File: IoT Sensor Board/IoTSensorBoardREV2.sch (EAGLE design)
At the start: 29 parts, among them Q1 BCW32SMD, Q2 BCW32SMD, U2 3.3V

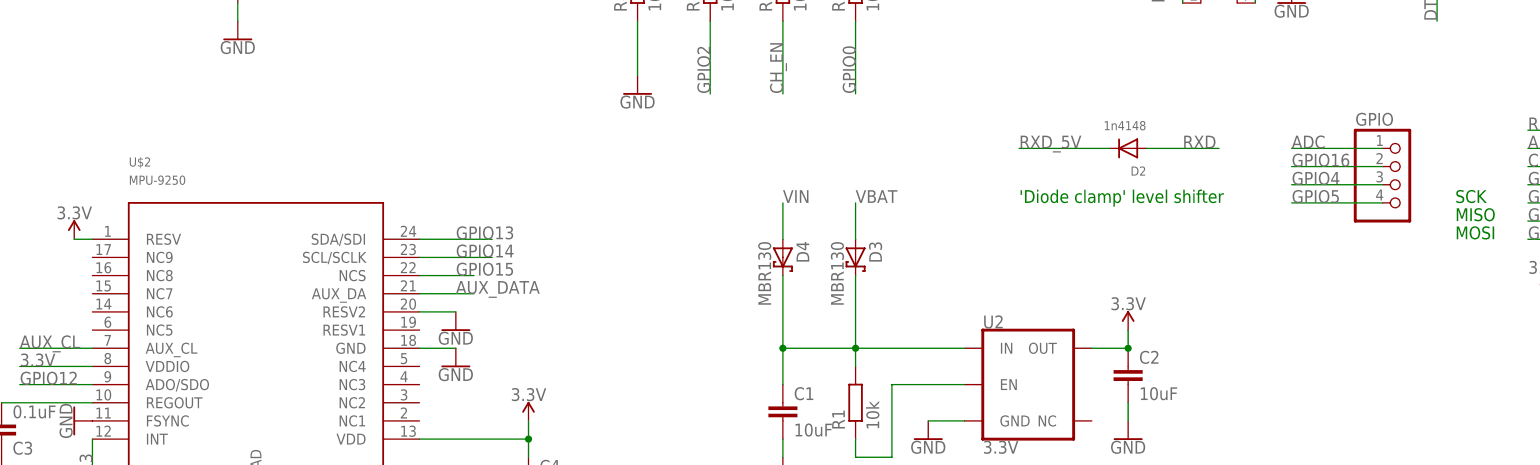
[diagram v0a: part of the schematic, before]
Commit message: Updated REV2
Silkscreen improved
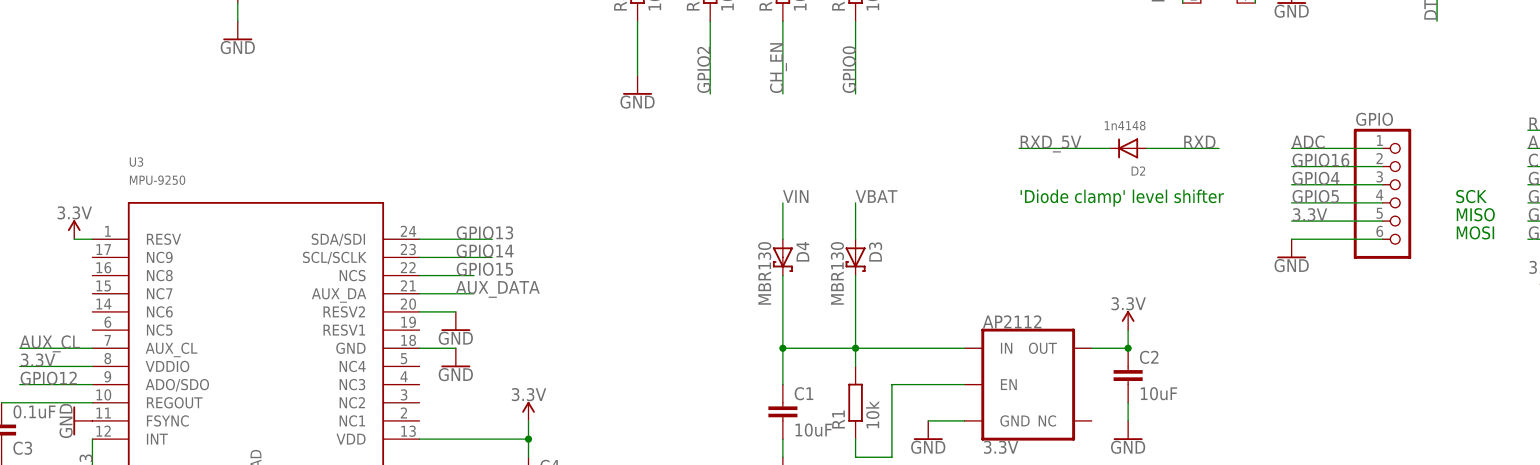
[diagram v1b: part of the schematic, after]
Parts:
- GPIO: device pinhead:PINHD-1X4 -> pinhead:PINHD-1X6
- renumbered U$2 to U3, U2 to AP2112, X1 to ESP-12
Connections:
- net 3.3V: now also GPIO.5
- net GND: now also GPIO.6
